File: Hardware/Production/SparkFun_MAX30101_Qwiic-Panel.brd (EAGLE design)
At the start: 123.2 x 175 mm, 1565 parts, among them J1 PTH, J101 PTH, J102 QWIIC_RA, J104 QWIIC_RA, J106 PTH, J107 QWIIC_RA, J109 QWIIC_RA, J11 PTH, J111 PTH, J112 QWIIC_RA, J114 QWIIC_RA, J116 PTH, J117 QWIIC_RA, J119 QWIIC_RA, J12 QWIIC_RA, J14 QWIIC_RA, J16 PTH, J17 QWIIC_RA, J19 QWIIC_RA, J21 PTH, J22 QWIIC_RA, J24 QWIIC_RA, J26 PTH, J27 QWIIC_RA, J29 QWIIC_RA, J3 QWIIC_RA, J31 PTH, J32 QWIIC_RA, J34 QWIIC_RA, J36 PTH, J37 QWIIC_RA, J39 QWIIC_RA, J41 PTH, J42 QWIIC_RA, J44 QWIIC_RA, J46 PTH, J47 QWIIC_RA, J49 QWIIC_RA, J5 QWIIC_RA, J51 PTH, J52 QWIIC_RA, J54 QWIIC_RA, J56 PTH, J57 QWIIC_RA, J59 QWIIC_RA, J6 PTH, J61 PTH, J62 QWIIC_RA, J64 QWIIC_RA, J66 PTH, J67 QWIIC_RA, J69 QWIIC_RA, J7 QWIIC_RA, J71 PTH, J72 QWIIC_RA, J74 QWIIC_RA, J76 PTH, J77 QWIIC_RA, J79 QWIIC_RA, J81 PTH, J82 QWIIC_RA, J84 QWIIC_RA, J86 PTH, J87 QWIIC_RA, J89 QWIIC_RA, J9 QWIIC_RA, J91 PTH, J92 QWIIC_RA, J94 QWIIC_RA, J96 PTH, J97 QWIIC_RA, J99 QWIIC_RA, Q1 20V/0.2A/8MHz/1.2Ω/1Vth, Q10 20V/0.2A/8MHz/1.2Ω/1Vth, Q11 20V/0.2A/8MHz/1.2Ω/1Vth, Q12 20V/0.2A/8MHz/1.2Ω/1Vth, Q13 20V/0.2A/8MHz/1.2Ω/1Vth, Q14 20V/0.2A/8MHz/1.2Ω/1Vth, Q15 20V/0.2A/8MHz/1.2Ω/1Vth, Q16 20V/0.2A/8MHz/1.2Ω/1Vth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

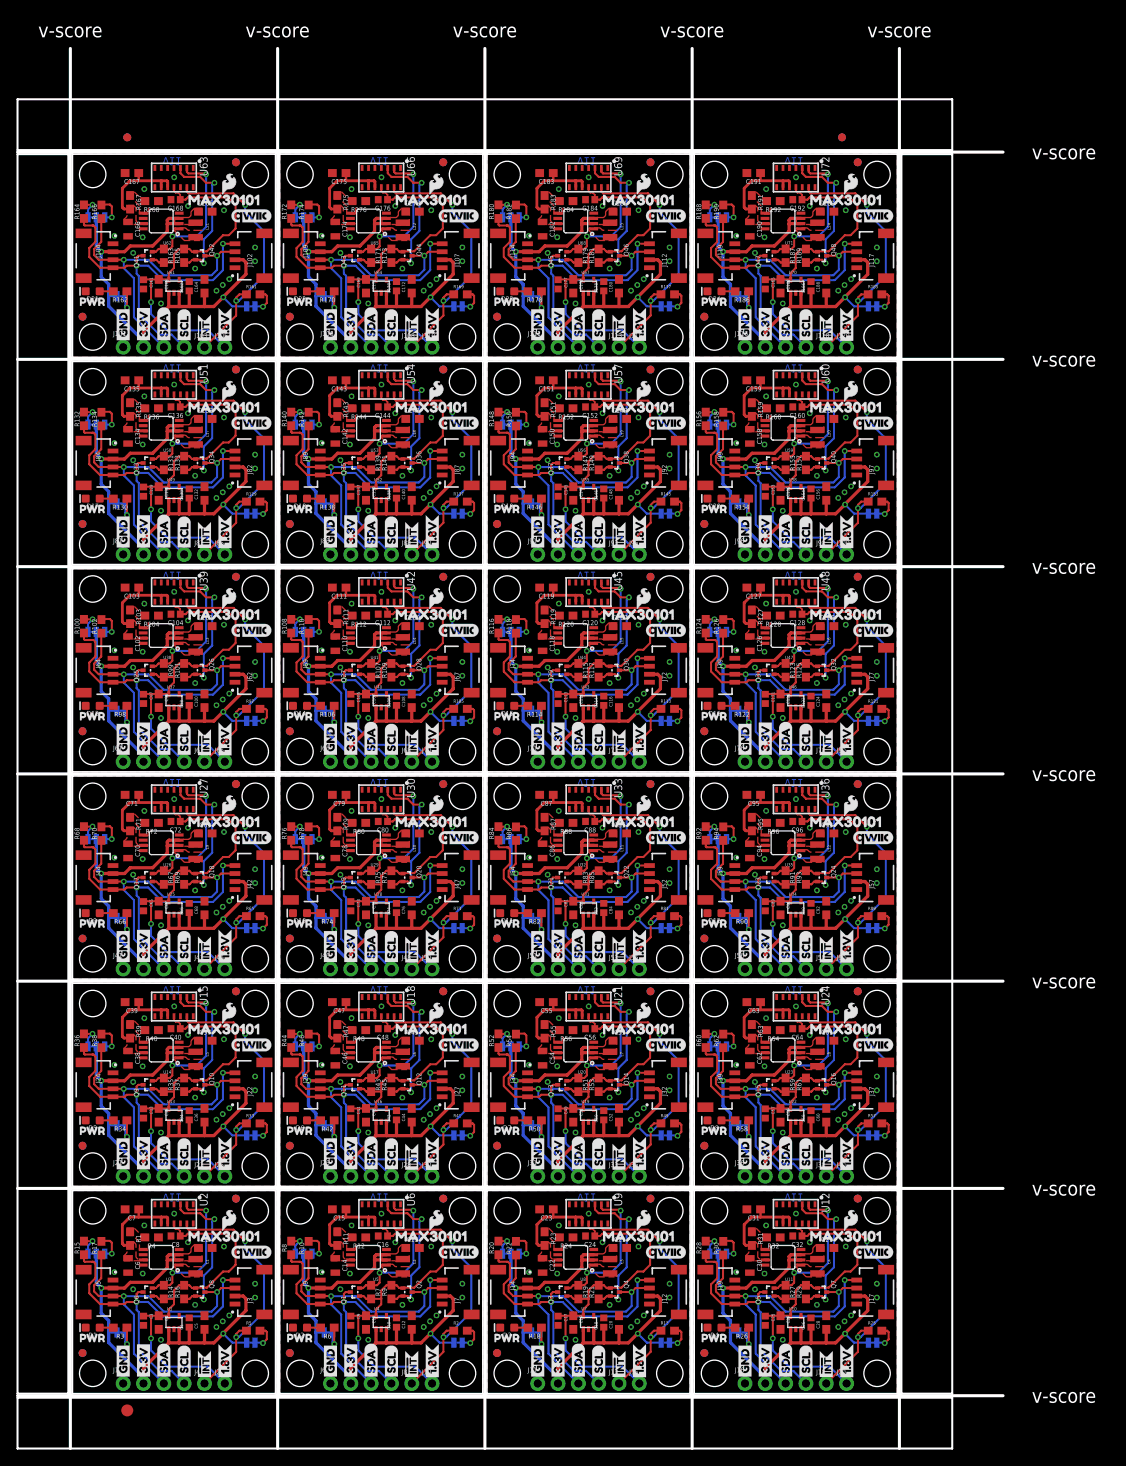
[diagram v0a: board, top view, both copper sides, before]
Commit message: Production panel updated to v12
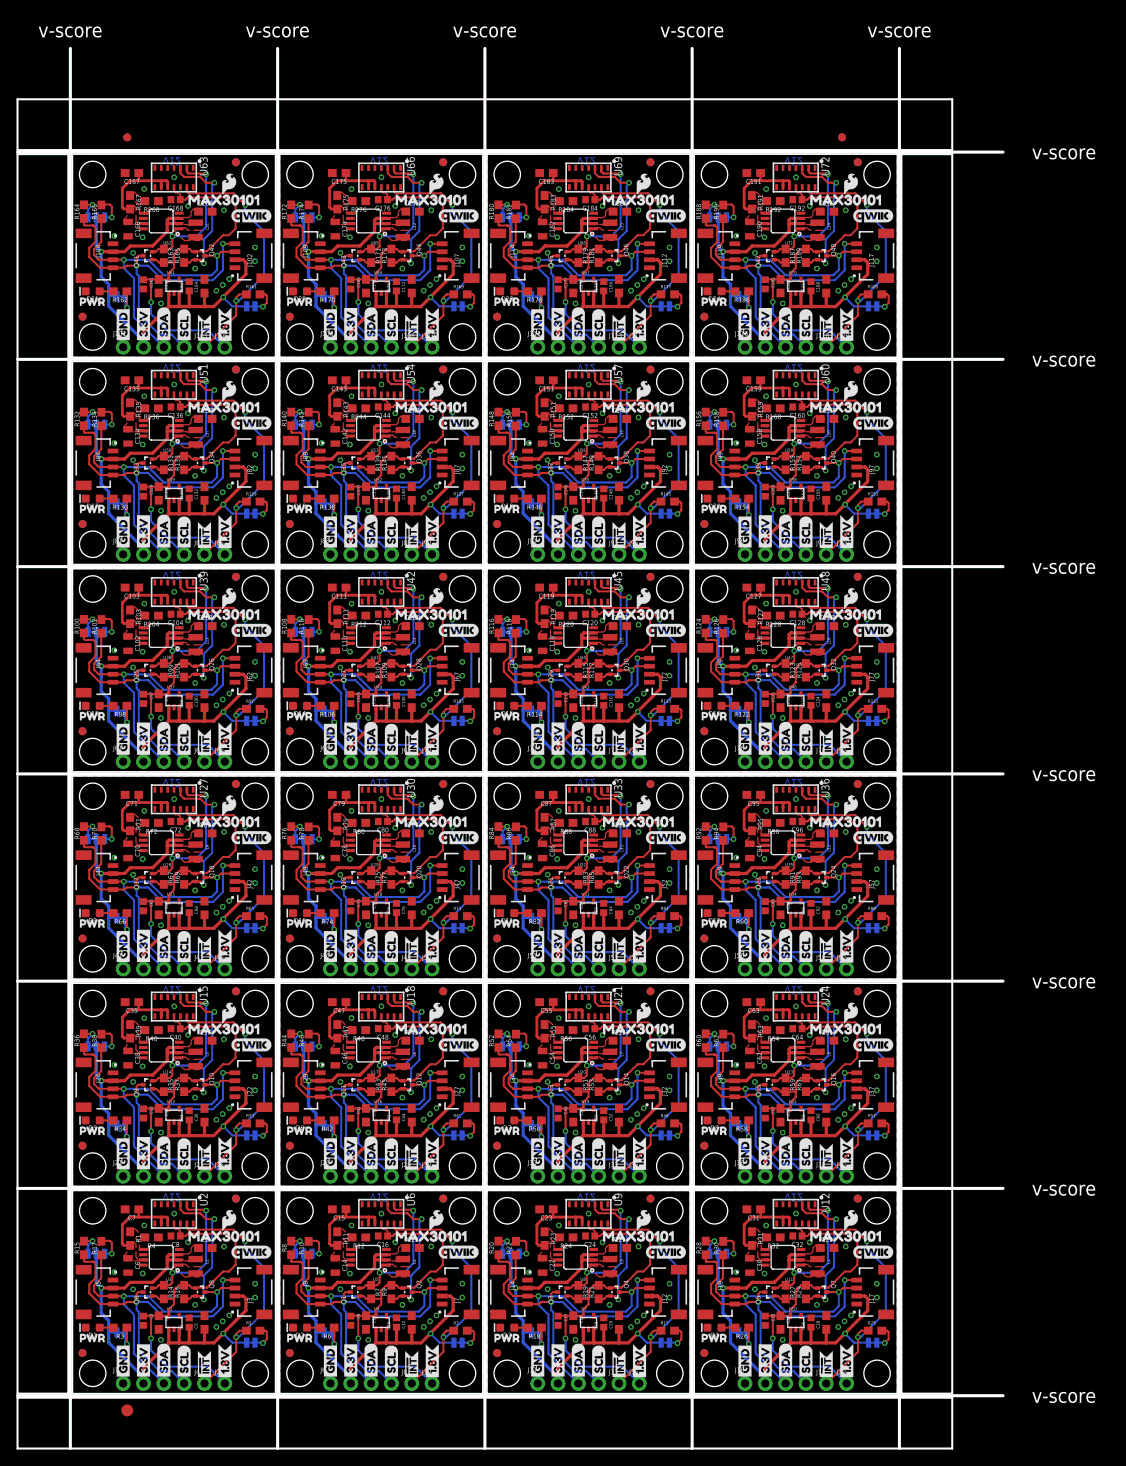
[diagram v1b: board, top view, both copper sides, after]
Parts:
- removed U$505, U$506, U$527, U$528: (no value), buzzard_labels (10):1#8V0
- removed U$507, U$509: (no value), Labels:INT#-[<-04
- removed U$508, U$514: (no value), Labels:SCL-[)
- removed U$510, U$511: (no value), Labels:3.3V
- removed U$512, U$513: (no value), Labels:GND-04
- removed U$515, U$516: (no value), Labels:SDA-[)
- removed U$517: (no value), Labels:INT-()-04
- removed U$518: (no value), Labels:I_SUPER2_C-()-04
- removed U$519: (no value), buzzard_labels (5):LED0
- removed U$520, U$524: (no value), buzzard_labels (7):MAX301010
- removed U$521: (no value), SparkFun-Aesthetics:QWIIC_5.5MM
- removed U$522: (no value), buzzard_labels (7):PARTICLE1
- removed U$523: (no value), buzzard_labels (7):SENSOR2
- removed U$525: (no value), buzzard_labels (9):ADR#_0X570
- removed U$526: (no value), SparkFun-Buzzard:PWR_TO
- U$1, U$399, U$441: device Labels:INT#-[<-04 -> buzzard_labels:PHOTODETECTOR3
- U$100, U$56: device Labels:I_SUPER2_C-()-04 -> buzzard_labels (7):MAX301010
- U$101: device buzzard_labels (5):LED0 -> buzzard_labels (9):ADR#_0X570
- U$102, U$480: device buzzard_labels (7):MAX301010 -> SparkFun-Buzzard:PWR_TO
- U$103, U$125: device SparkFun-Aesthetics:QWIIC_5.5MM -> buzzard_labels (10):1#8V0
- U$104, U$82: device buzzard_labels (7):PARTICLE1 -> buzzard_labels (10):1#8V0
- U$105: device buzzard_labels (7):SENSOR2 -> buzzard_labels:PHOTODETECTOR3
- U$106, U$150, U$190, U$234: device buzzard_labels (7):MAX301010 -> Labels:INT#-[<-04
- U$107, U$239: device buzzard_labels (9):ADR#_0X570 -> Labels:SCL-[)
- U$108, U$64: device SparkFun-Buzzard:PWR_TO -> Labels:INT#-[<-04
- U$109, U$110, U$131, U$88: device buzzard_labels (10):1#8V0 -> Labels:3.3V
- U$111, U$133, U$69, U$91: device Labels:INT#-[<-04 -> Labels:GND-04
- U$112, U$426, U$448, U$90: device Labels:SCL-[) -> Labels:GND-04
- U$113, U$155, U$443, U$485, U$5: device Labels:INT#-[<-04 -> Labels:SCL-[)
- U$114, U$115, U$136, U$93: device Labels:3.3V -> Labels:SDA-[)
- U$116, U$95: device Labels:GND-04 -> Labels:INT-()-04
- U$117, U$138: device Labels:GND-04 -> Labels:I_SUPER2_C-()-04
- U$118, U$244: device Labels:SCL-[) -> buzzard_labels (5):LED0
- U$119, U$142, U$163, U$98: device Labels:SDA-[) -> buzzard_labels (7):MAX301010
- U$120, U$141: device Labels:SDA-[) -> SparkFun-Aesthetics:QWIIC_5.5MM
- U$121, U$77: device Labels:INT-()-04 -> buzzard_labels (7):MAX301010
- U$122: device Labels:I_SUPER2_C-()-04 -> buzzard_labels (9):ADR#_0X570
- U$123: device buzzard_labels (5):LED0 -> SparkFun-Buzzard:PWR_TO
- U$124, U$146, U$40, U$502, U$62: device buzzard_labels (7):MAX301010 -> buzzard_labels (10):1#8V0
- U$126: device buzzard_labels (7):PARTICLE1 -> buzzard_labels:PHOTODETECTOR3
- U$127, U$171: device buzzard_labels (7):SENSOR2 -> Labels:INT#-[<-04
- U$128, U$212, U$260, U$344: device buzzard_labels (7):MAX301010 -> Labels:SCL-[)
- U$129, U$85: device buzzard_labels (9):ADR#_0X570 -> Labels:INT#-[<-04
- U$130, U$152: device SparkFun-Buzzard:PWR_TO -> Labels:3.3V
- U$132, U$153, U$154, U$175: device buzzard_labels (10):1#8V0 -> Labels:GND-04
- U$135, U$157, U$177, U$199: device Labels:INT#-[<-04 -> Labels:SDA-[)
- U$137, U$158: device Labels:3.3V -> Labels:INT-()-04
- U$139, U$160: device Labels:GND-04 -> buzzard_labels (5):LED0
- U$140, U$184, U$266, U$310: device Labels:SCL-[) -> buzzard_labels (7):MAX301010
- U$143: device Labels:INT-()-04 -> buzzard_labels (9):ADR#_0X570
- U$144: device Labels:I_SUPER2_C-()-04 -> SparkFun-Buzzard:PWR_TO
- U$145, U$167: device buzzard_labels (5):LED0 -> buzzard_labels (10):1#8V0
- U$147: device SparkFun-Aesthetics:QWIIC_5.5MM -> buzzard_labels:PHOTODETECTOR3
- U$148, U$192: device buzzard_labels (7):PARTICLE1 -> Labels:INT#-[<-04
- U$149, U$281: device buzzard_labels (7):SENSOR2 -> Labels:SCL-[)
- U$151, U$173: device buzzard_labels (9):ADR#_0X570 -> Labels:3.3V
- U$156, U$178, U$30, U$492, U$52: device Labels:SCL-[) -> Labels:SDA-[)
- U$159, U$180: device Labels:3.3V -> Labels:I_SUPER2_C-()-04
- U$161, U$182, U$205, U$226: device Labels:GND-04 -> buzzard_labels (7):MAX301010
- U$162, U$288: device Labels:SCL-[) -> SparkFun-Aesthetics:QWIIC_5.5MM
- U$164, U$185: device Labels:SDA-[) -> buzzard_labels (9):ADR#_0X570
- U$165: device Labels:INT-()-04 -> SparkFun-Buzzard:PWR_TO
- U$166, U$188: device Labels:I_SUPER2_C-()-04 -> buzzard_labels (10):1#8V0
- U$168, U$84: device buzzard_labels (7):MAX301010 -> buzzard_labels:PHOTODETECTOR3
- U$169, U$213: device SparkFun-Aesthetics:QWIIC_5.5MM -> Labels:INT#-[<-04
- U$17, U$214, U$236: device buzzard_labels (7):PARTICLE1 -> Labels:3.3V
- U$170, U$302: device buzzard_labels (7):PARTICLE1 -> Labels:SCL-[)
- U$172, U$194, U$256, U$278: device buzzard_labels (7):MAX301010 -> Labels:3.3V
- U$174, U$196: device SparkFun-Buzzard:PWR_TO -> Labels:GND-04
- U$176, U$197, U$44, U$65: device buzzard_labels (10):1#8V0 -> Labels:SCL-[)
- U$179, U$221: device Labels:INT#-[<-04 -> Labels:INT-()-04
- U$18, U$193, U$215: device buzzard_labels (7):SENSOR2 -> Labels:3.3V
- U$181, U$202: device Labels:3.3V -> buzzard_labels (5):LED0
- U$183, U$204: device Labels:GND-04 -> SparkFun-Aesthetics:QWIIC_5.5MM
- U$186, U$207: device Labels:SDA-[) -> SparkFun-Buzzard:PWR_TO
- U$187, U$209: device Labels:INT-()-04 -> buzzard_labels (10):1#8V0
- U$189: device buzzard_labels (5):LED0 -> buzzard_labels:PHOTODETECTOR3
- U$191, U$323: device SparkFun-Aesthetics:QWIIC_5.5MM -> Labels:SCL-[)
- U$195, U$217: device buzzard_labels (9):ADR#_0X570 -> Labels:GND-04
- U$198, U$219, U$220, U$241: device buzzard_labels (10):1#8V0 -> Labels:SDA-[)
- U$2, U$316, U$360, U$442, U$486: device Labels:SCL-[) -> Labels:INT#-[<-04
- U$200, U$74: device Labels:SCL-[) -> Labels:INT-()-04
- U$201, U$243: device Labels:INT#-[<-04 -> Labels:I_SUPER2_C-()-04
- U$203, U$224, U$247, U$268: device Labels:3.3V -> buzzard_labels (7):MAX301010
- U$206, U$332: device Labels:SCL-[) -> buzzard_labels (9):ADR#_0X570
- U$208, U$229, U$230, U$251: device Labels:SDA-[) -> buzzard_labels (10):1#8V0
- U$210: device Labels:I_SUPER2_C-()-04 -> buzzard_labels:PHOTODETECTOR3
- U$211, U$255: device buzzard_labels (5):LED0 -> Labels:INT#-[<-04
- U$216, U$238, U$300, U$322: device buzzard_labels (7):MAX301010 -> Labels:GND-04
- U$218, U$86: device SparkFun-Buzzard:PWR_TO -> Labels:SCL-[)
- U$222, U$96: device Labels:SCL-[) -> Labels:I_SUPER2_C-()-04
- U$223, U$265: device Labels:INT#-[<-04 -> buzzard_labels (5):LED0
- U$225, U$246: device Labels:3.3V -> SparkFun-Aesthetics:QWIIC_5.5MM
- U$227, U$248: device Labels:GND-04 -> buzzard_labels (9):ADR#_0X570
- U$228, U$354: device Labels:SCL-[) -> SparkFun-Buzzard:PWR_TO
- U$231: device Labels:INT-()-04 -> buzzard_labels:PHOTODETECTOR3
- U$232, U$276: device Labels:I_SUPER2_C-()-04 -> Labels:INT#-[<-04
- U$233, U$365: device buzzard_labels (5):LED0 -> Labels:SCL-[)
- U$235, U$257: device SparkFun-Aesthetics:QWIIC_5.5MM -> Labels:3.3V
- U$237, U$259: device buzzard_labels (7):SENSOR2 -> Labels:GND-04
- U$240, U$262: device SparkFun-Buzzard:PWR_TO -> Labels:SDA-[)
- U$242, U$263: device buzzard_labels (10):1#8V0 -> Labels:INT-()-04
- U$245, U$287, U$289, U$331: device Labels:INT#-[<-04 -> buzzard_labels (7):MAX301010
- U$249, U$270: device Labels:GND-04 -> SparkFun-Buzzard:PWR_TO
- U$25, U$48, U$489, U$49, U$70: device Labels:3.3V -> Labels:GND-04
- U$250, U$272, U$376, U$398: device Labels:SCL-[) -> buzzard_labels (10):1#8V0
- U$252, U$273: device Labels:SDA-[) -> buzzard_labels:PHOTODETECTOR3
- U$253, U$297: device Labels:INT-()-04 -> Labels:INT#-[<-04
- U$254, U$386: device Labels:I_SUPER2_C-()-04 -> Labels:SCL-[)
- U$258, U$280: device buzzard_labels (7):PARTICLE1 -> Labels:GND-04
- U$261, U$283: device buzzard_labels (9):ADR#_0X570 -> Labels:SDA-[)
- U$264, U$285: device buzzard_labels (10):1#8V0 -> Labels:I_SUPER2_C-()-04
- U$267, U$309: device Labels:INT#-[<-04 -> SparkFun-Aesthetics:QWIIC_5.5MM
- U$269, U$290: device Labels:3.3V -> buzzard_labels (9):ADR#_0X570
- U$271, U$292, U$293, U$314: device Labels:GND-04 -> buzzard_labels (10):1#8V0
- U$274, U$295, U$318, U$339: device Labels:SDA-[) -> Labels:INT#-[<-04
- U$275, U$407: device Labels:INT-()-04 -> Labels:SCL-[)
- U$277, U$299: device buzzard_labels (5):LED0 -> Labels:3.3V
- U$279, U$301: device SparkFun-Aesthetics:QWIIC_5.5MM -> Labels:GND-04
- U$282, U$304, U$366, U$388: device buzzard_labels (7):MAX301010 -> Labels:SDA-[)
- U$284: device SparkFun-Buzzard:PWR_TO -> Labels:INT-()-04
- U$286, U$307: device buzzard_labels (10):1#8V0 -> buzzard_labels (5):LED0
- U$29, U$359, U$380, U$491, U$50: device Labels:GND-04 -> Labels:SCL-[)
- U$291, U$312: device Labels:3.3V -> SparkFun-Buzzard:PWR_TO
- U$294, U$420: device Labels:SCL-[) -> buzzard_labels:PHOTODETECTOR3
- U$296, U$317, U$428, U$449: device Labels:SDA-[) -> Labels:SCL-[)
- U$298, U$320: device Labels:I_SUPER2_C-()-04 -> Labels:3.3V
- U$303, U$325: device buzzard_labels (7):SENSOR2 -> Labels:SDA-[)
- U$305: device buzzard_labels (9):ADR#_0X570 -> Labels:INT-()-04
- U$306: device SparkFun-Buzzard:PWR_TO -> Labels:I_SUPER2_C-()-04
- U$308, U$329, U$352, U$373: device buzzard_labels (10):1#8V0 -> buzzard_labels (7):MAX301010
- U$311, U$353: device Labels:INT#-[<-04 -> buzzard_labels (9):ADR#_0X570
- U$313, U$334, U$335, U$356: device Labels:3.3V -> buzzard_labels (10):1#8V0
- U$315, U$336: device Labels:GND-04 -> buzzard_labels:PHOTODETECTOR3
- U$319, U$341: device Labels:INT-()-04 -> Labels:3.3V
- U$32, U$494, U$53: device Labels:SDA-[) -> Labels:INT-()-04
- U$321, U$343: device buzzard_labels (5):LED0 -> Labels:GND-04
- U$324, U$346: device buzzard_labels (7):PARTICLE1 -> Labels:SDA-[)
- U$326, U$410: device buzzard_labels (7):MAX301010 -> Labels:INT-()-04
- U$327: device buzzard_labels (9):ADR#_0X570 -> Labels:I_SUPER2_C-()-04
- U$328: device SparkFun-Buzzard:PWR_TO -> buzzard_labels (5):LED0
- U$33, U$495: device Labels:INT-()-04 -> Labels:I_SUPER2_C-()-04
- U$330, U$351: device buzzard_labels (10):1#8V0 -> SparkFun-Aesthetics:QWIIC_5.5MM
- U$333, U$375: device Labels:INT#-[<-04 -> SparkFun-Buzzard:PWR_TO
- U$337, U$358, U$381, U$402: device Labels:GND-04 -> Labels:INT#-[<-04
- U$34, U$496: device Labels:I_SUPER2_C-()-04 -> buzzard_labels (5):LED0
- U$340, U$361, U$362, U$383: device Labels:SDA-[) -> Labels:3.3V
- U$342, U$364: device Labels:I_SUPER2_C-()-04 -> Labels:GND-04
- U$345, U$367: device SparkFun-Aesthetics:QWIIC_5.5MM -> Labels:SDA-[)
- U$347: device buzzard_labels (7):SENSOR2 -> Labels:INT-()-04
- U$348, U$432: device buzzard_labels (7):MAX301010 -> Labels:I_SUPER2_C-()-04
- U$349: device buzzard_labels (9):ADR#_0X570 -> buzzard_labels (5):LED0
- U$35, U$497, U$79: device buzzard_labels (5):LED0 -> buzzard_labels (7):MAX301010
- U$350, U$394: device SparkFun-Buzzard:PWR_TO -> buzzard_labels (7):MAX301010
- U$355, U$377, U$397, U$419: device Labels:INT#-[<-04 -> buzzard_labels (10):1#8V0
- U$357, U$378: device Labels:3.3V -> buzzard_labels:PHOTODETECTOR3
- U$36, U$414, U$498: device buzzard_labels (7):MAX301010 -> SparkFun-Aesthetics:QWIIC_5.5MM
- U$363, U$385: device Labels:INT-()-04 -> Labels:GND-04
- U$368: device buzzard_labels (7):PARTICLE1 -> Labels:INT-()-04
- U$369: device buzzard_labels (7):SENSOR2 -> Labels:I_SUPER2_C-()-04
- U$37, U$455, U$499: device SparkFun-Aesthetics:QWIIC_5.5MM -> buzzard_labels (7):MAX301010
- U$370, U$454: device buzzard_labels (7):MAX301010 -> buzzard_labels (5):LED0
- U$371, U$415: device buzzard_labels (9):ADR#_0X570 -> buzzard_labels (7):MAX301010
- U$372: device SparkFun-Buzzard:PWR_TO -> SparkFun-Aesthetics:QWIIC_5.5MM
- U$374, U$395: device buzzard_labels (10):1#8V0 -> buzzard_labels (9):ADR#_0X570
- U$379, U$400, U$423, U$444, U$6: device Labels:3.3V -> Labels:INT#-[<-04
- U$38, U$500: device buzzard_labels (7):PARTICLE1 -> buzzard_labels (9):ADR#_0X570
- U$382, U$404, U$46, U$68: device Labels:SCL-[) -> Labels:3.3V
- U$384, U$405, U$406, U$427: device Labels:SDA-[) -> Labels:GND-04
- U$387, U$409: device buzzard_labels (5):LED0 -> Labels:SDA-[)
- U$389: device SparkFun-Aesthetics:QWIIC_5.5MM -> Labels:INT-()-04
- U$39, U$501: device buzzard_labels (7):SENSOR2 -> SparkFun-Buzzard:PWR_TO
- U$390: device buzzard_labels (7):PARTICLE1 -> Labels:I_SUPER2_C-()-04
- U$391: device buzzard_labels (7):SENSOR2 -> buzzard_labels (5):LED0
- U$393: device buzzard_labels (9):ADR#_0X570 -> SparkFun-Aesthetics:QWIIC_5.5MM
- U$396, U$417: device buzzard_labels (10):1#8V0 -> SparkFun-Buzzard:PWR_TO
- U$401, U$422, U$71, U$92: device Labels:3.3V -> Labels:SCL-[)
- U$403, U$424, U$425, U$446: device Labels:GND-04 -> Labels:3.3V
- U$408, U$430: device Labels:I_SUPER2_C-()-04 -> Labels:SDA-[)
- U$41, U$481, U$503: device buzzard_labels (9):ADR#_0X570 -> buzzard_labels (10):1#8V0
- U$411: device SparkFun-Aesthetics:QWIIC_5.5MM -> Labels:I_SUPER2_C-()-04
- U$412: device buzzard_labels (7):PARTICLE1 -> buzzard_labels (5):LED0
- U$413, U$457: device buzzard_labels (7):SENSOR2 -> buzzard_labels (7):MAX301010
- U$416: device SparkFun-Buzzard:PWR_TO -> buzzard_labels (9):ADR#_0X570
- U$42, U$504: device SparkFun-Buzzard:PWR_TO -> buzzard_labels:PHOTODETECTOR3
- U$429, U$451: device Labels:INT-()-04 -> Labels:SDA-[)
- U$43, U$484, U$66, U$87: device buzzard_labels (10):1#8V0 -> Labels:INT#-[<-04
- U$431: device buzzard_labels (5):LED0 -> Labels:INT-()-04
- U$433: device SparkFun-Aesthetics:QWIIC_5.5MM -> buzzard_labels (5):LED0
- U$434, U$478: device buzzard_labels (7):PARTICLE1 -> buzzard_labels (7):MAX301010
- U$435: device buzzard_labels (7):SENSOR2 -> SparkFun-Aesthetics:QWIIC_5.5MM
- U$452: device Labels:I_SUPER2_C-()-04 -> Labels:INT-()-04
- U$453: device buzzard_labels (5):LED0 -> Labels:I_SUPER2_C-()-04
- U$456: device buzzard_labels (7):PARTICLE1 -> SparkFun-Aesthetics:QWIIC_5.5MM
- U$458, U$80: device buzzard_labels (7):MAX301010 -> buzzard_labels (9):ADR#_0X570
- U$459: device buzzard_labels (9):ADR#_0X570 -> SparkFun-Buzzard:PWR_TO
- U$460, U$482: device SparkFun-Buzzard:PWR_TO -> buzzard_labels (10):1#8V0
- U$462, U$483: device buzzard_labels (10):1#8V0 -> buzzard_labels:PHOTODETECTOR3
- U$47, U$487, U$67, U$89: device Labels:INT#-[<-04 -> Labels:3.3V
- U$479: device buzzard_labels (7):SENSOR2 -> buzzard_labels (9):ADR#_0X570
- U$51, U$72, U$73, U$94: device Labels:GND-04 -> Labels:SDA-[)
- U$54, U$75: device Labels:SDA-[) -> Labels:I_SUPER2_C-()-04
- U$55: device Labels:INT-()-04 -> buzzard_labels (5):LED0
- U$57: device buzzard_labels (5):LED0 -> SparkFun-Aesthetics:QWIIC_5.5MM
- U$59: device SparkFun-Aesthetics:QWIIC_5.5MM -> buzzard_labels (9):ADR#_0X570
- U$60: device buzzard_labels (7):PARTICLE1 -> SparkFun-Buzzard:PWR_TO
- U$61, U$83: device buzzard_labels (7):SENSOR2 -> buzzard_labels (10):1#8V0
- U$63: device buzzard_labels (9):ADR#_0X570 -> buzzard_labels:PHOTODETECTOR3
- U$76, U$97: device Labels:SDA-[) -> buzzard_labels (5):LED0
- U$78: device Labels:I_SUPER2_C-()-04 -> SparkFun-Aesthetics:QWIIC_5.5MM
- U$81: device SparkFun-Aesthetics:QWIIC_5.5MM -> SparkFun-Buzzard:PWR_TO
- U$99: device Labels:INT-()-04 -> SparkFun-Aesthetics:QWIIC_5.5MM
- moved U$264 100.2 mm to (4.95, 93.4), turned to 0 degrees
- moved U$341 95.3 mm to (8.89, 105.3), turned to 90 degrees
- moved U$348 94.8 mm to (4.95, 119.4)
- moved U$175 94.1 mm to (6.35, 53.5)
- moved U$429 92.8 mm to (11.4, 131.2), flipped to the top, turned to 90 degrees
- moved U$258 92.5 mm to (6.35, 79.4), turned to 90 degrees
- moved U$351 92.1 mm to (13.0, 117.6), flipped to the bottom, turned to 0 degrees
- moved U$88 91.6 mm to (8.89, 27.6), flipped to the top
- moved U$349 89.5 mm to (8.46, 113.0)
- moved U$434 89.3 mm to (13.3, 149.2), flipped to the top
- moved U$426 89.2 mm to (6.35, 131.2), flipped to the bottom
- moved U$432 88.8 mm to (4.95, 145.3), flipped to the bottom
- moved U$352 88.2 mm to (18.5, 119.9), turned to 0 degrees
- moved U$172 88.1 mm to (8.89, 53.5), flipped to the top, turned to 90 degrees
- moved U$253 87.8 mm to (16.5, 79.1), flipped to the top, turned to 90 degrees
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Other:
- board text added: "v12"
- board text removed: "v11"
